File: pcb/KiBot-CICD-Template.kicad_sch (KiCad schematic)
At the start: 1 part

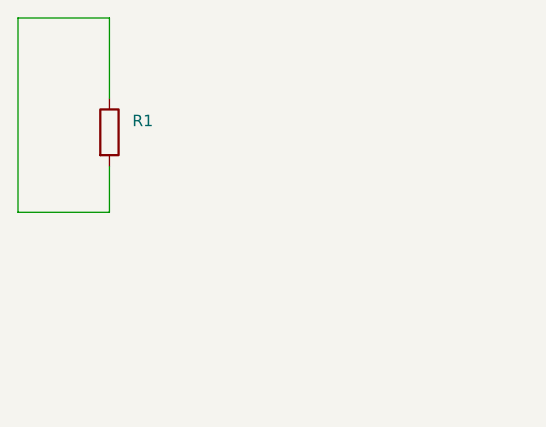
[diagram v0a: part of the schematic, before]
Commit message: fix string replace
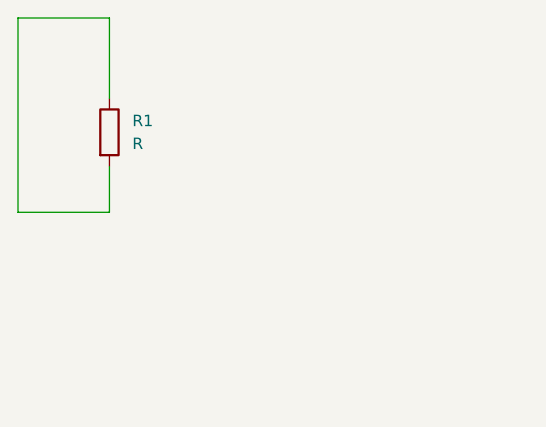
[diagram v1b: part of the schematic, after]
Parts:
- R1: value (none) -> R
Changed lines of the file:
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@@
   (title_block
     (title "KiBot-CICD-Template")
-    (date "@date@")
-    (rev "@version@")
+    (date "${date}")
+    (rev "${version}")
     (company "nerdyscout")
     (comment 4 "CERN Open Hardware Licence v2.0")
@@
       (effects (font (size 1.27 1.27)) (justify left))
     )
-    (property "Value" "" (id 1) (at 111.76 111.7599 0)
+    (property "Value" "R" (id 1) (at 111.76 111.7599 0)
       (effects (font (size 1.27 1.27)) (justify left))
     )
